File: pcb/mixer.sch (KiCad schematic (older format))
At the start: 59 parts, among them J18 Conn_Coaxial, J19 Conn_Coaxial, T1 Transformer_1P_SS, T2 Transformer_1P_SS, T3 Transformer_1P_SS, T4 Transformer_1P_SS, U4 TLV3542IDR

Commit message: layout progress
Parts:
- J18, J19: footprint Connector_Coaxial:SMA_Amphenol_132289_EdgeMount -> Connector_Coaxial:SMA_Samtec_SMA-J-P-X-ST-EM1_EdgeMount
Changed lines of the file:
@@
 F 0 "J18" H 6428 2488 50  0000 C CNN
 F 1 "Conn_Coaxial" H 6428 2397 50  0000 C CNN
-F 2 "Connector_Coaxial:SMA_Amphenol_132289_EdgeMount" H 6500 2250 50  0001 C CNN
+F 2 "Connector_Coaxial:SMA_Samtec_SMA-J-P-X-ST-EM1_EdgeMount" H 6500 2250 50  0001 C CNN
 F 3 " ~" H 6500 2250 50  0001 C CNN
 	1    6500 2250
@@
 F 0 "J19" H 6828 5338 50  0000 C CNN
 F 1 "Conn_Coaxial" H 6828 5247 50  0000 C CNN
-F 2 "Connector_Coaxial:SMA_Amphenol_132289_EdgeMount" H 6900 5100 50  0001 C CNN
+F 2 "Connector_Coaxial:SMA_Samtec_SMA-J-P-X-ST-EM1_EdgeMount" H 6900 5100 50  0001 C CNN
 F 3 " ~" H 6900 5100 50  0001 C CNN
 	1    6900 5100

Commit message: Add SMA step model
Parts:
- J18, J19: footprint Connector_Coaxial:SMA_Samtec_SMA-J-P-X-ST-EM1_EdgeMount -> iq_siggen:SMA_Samtec_SMA-J-P-X-ST-EM1_EdgeMount_withSTEP
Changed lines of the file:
@@
 F 0 "J18" H 6428 2488 50  0000 C CNN
 F 1 "Conn_Coaxial" H 6428 2397 50  0000 C CNN
-F 2 "Connector_Coaxial:SMA_Samtec_SMA-J-P-X-ST-EM1_EdgeMount" H 6500 2250 50  0001 C CNN
+F 2 "iq_siggen:SMA_Samtec_SMA-J-P-X-ST-EM1_EdgeMount_withSTEP" H 6500 2250 50  0001 C CNN
 F 3 " ~" H 6500 2250 50  0001 C CNN
 	1    6500 2250
@@
 F 0 "J19" H 6828 5338 50  0000 C CNN
 F 1 "Conn_Coaxial" H 6828 5247 50  0000 C CNN
-F 2 "Connector_Coaxial:SMA_Samtec_SMA-J-P-X-ST-EM1_EdgeMount" H 6900 5100 50  0001 C CNN
+F 2 "iq_siggen:SMA_Samtec_SMA-J-P-X-ST-EM1_EdgeMount_withSTEP" H 6900 5100 50  0001 C CNN
 F 3 " ~" H 6900 5100 50  0001 C CNN
 	1    6900 5100

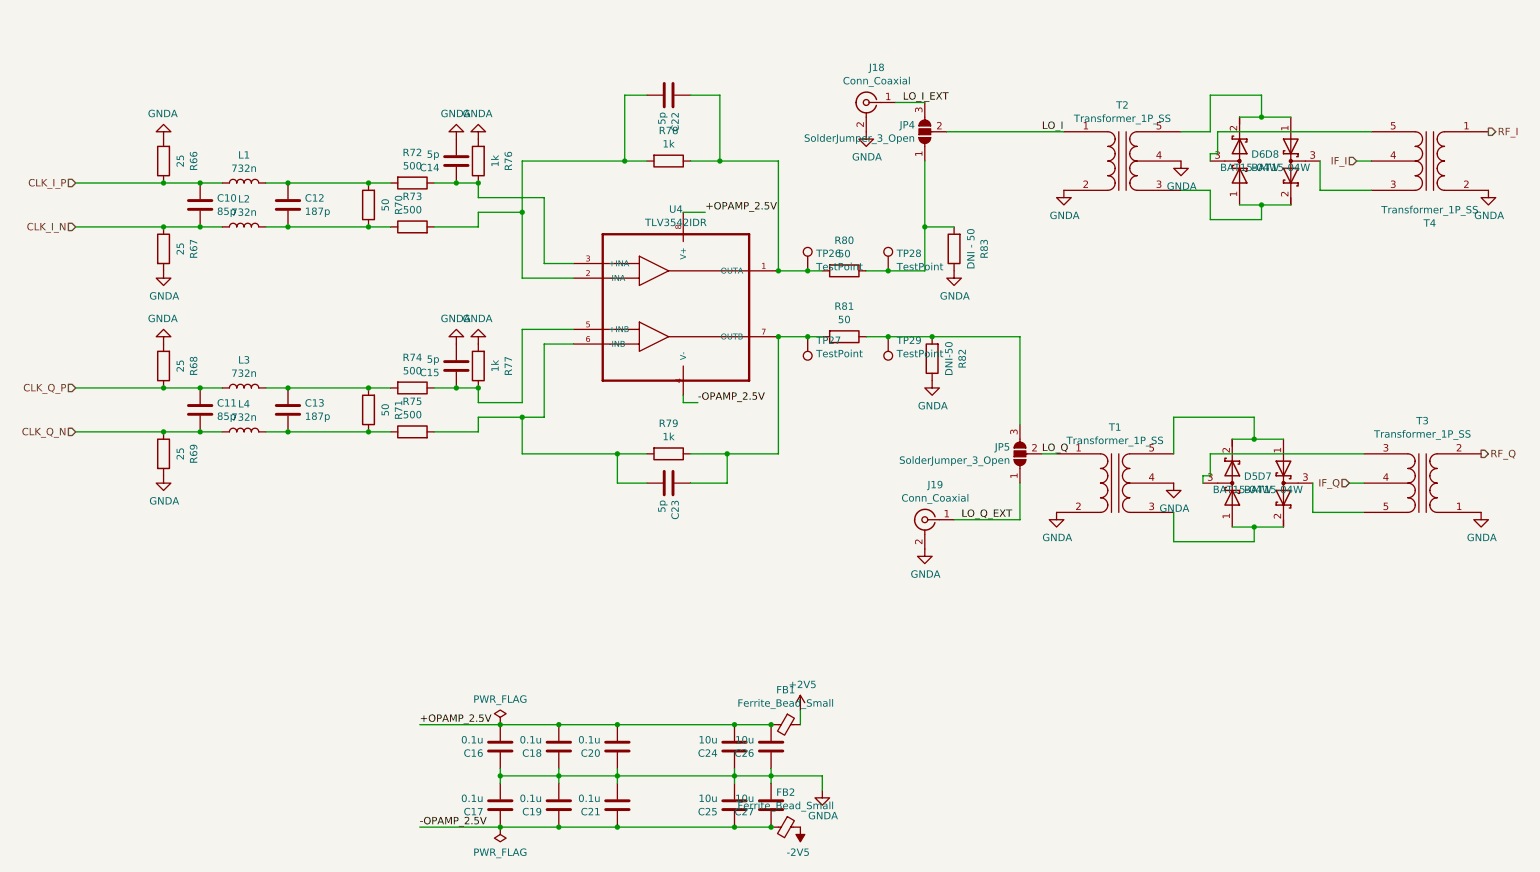
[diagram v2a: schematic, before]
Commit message: LO amp routing
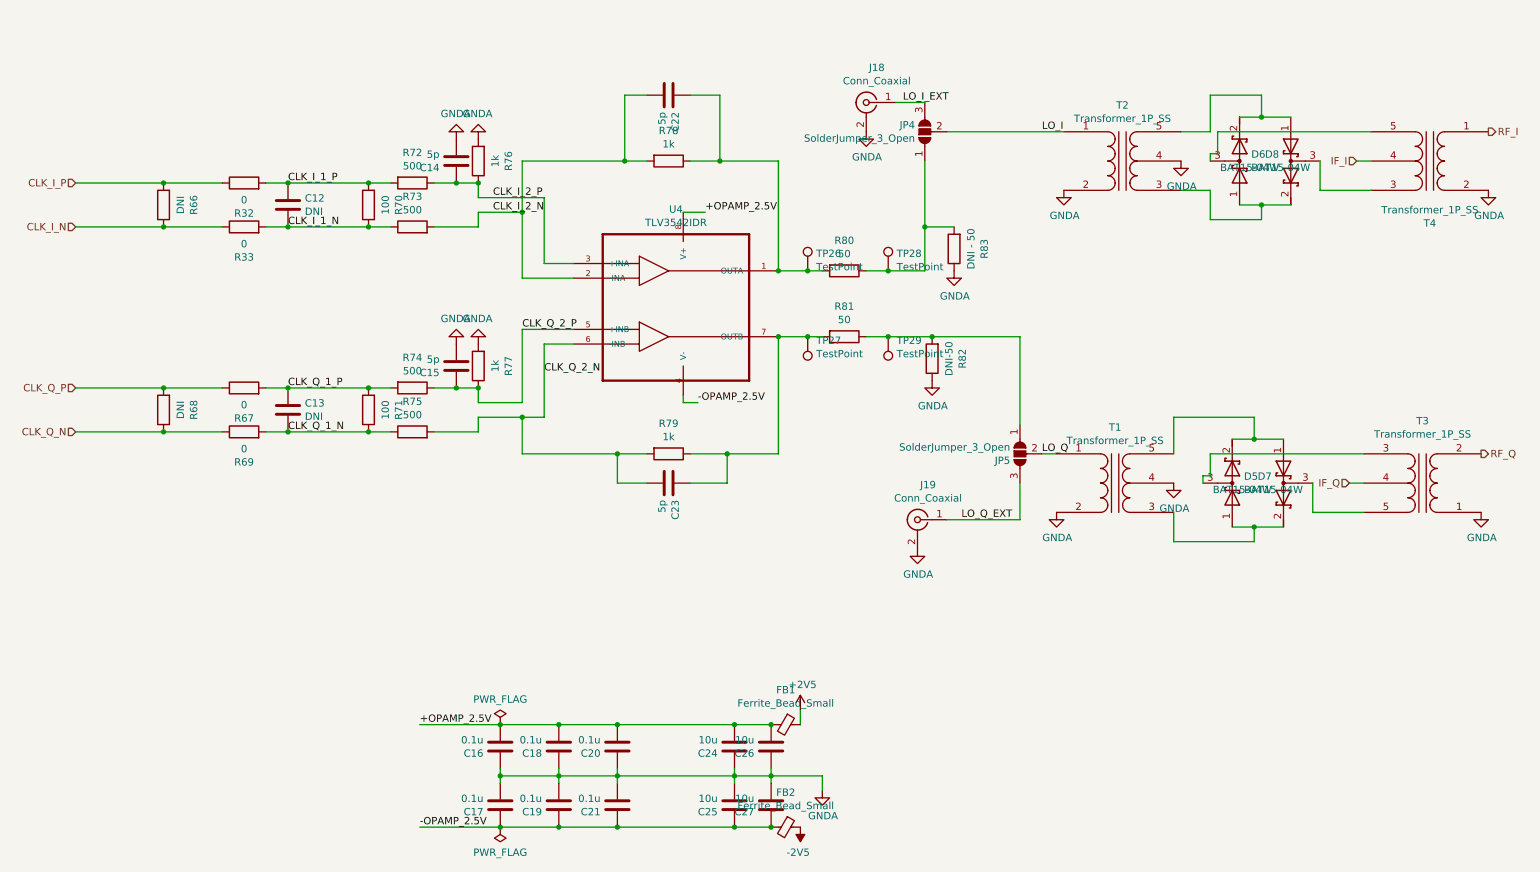
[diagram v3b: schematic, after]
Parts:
- removed C10, C11: 85p, Capacitor_SMD:C_0603_1608Metric, symbol Device:C
- removed L1, L2, L3, L4: 732n, Inductor_SMD:L_0603_1608Metric_Pad1.05x0.95mm_HandSolder, symbol Device:L
- added R32, R33: 0, Resistor_SMD:R_0603_1608Metric, symbol Device:R
- C12, C13: value 187p -> DNI
- JP4, JP5: footprint (none) -> iq_siggen:50ohm_solder_jumper
- R66, R68: value 25 -> DNI
- R67, R69: value 25 -> 0
- R70, R71: value 50 -> 100
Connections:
- net CLK_I_N: now also R66.1, R33.1; no longer R67.1
- net CLK_I_P: now also R66.2, R32.1; no longer R66.1
- net CLK_Q_N: now also R68.1
- net CLK_Q_P: now also R67.1, R68.2; no longer R68.1
- net GNDA: no longer R66.2, R67.2, R68.2, R69.2
- net LO_Q_EXT: now also JP5.3 (B); no longer JP5.1 (A)
- net CLK_I_2_N: now reaches C22.2, R73.2, R78.2, U4.2 (-INA)
- net CLK_I_2_P: now reaches C14.1, R72.1, R76.1, U4.3 (+INA)
- net CLK_Q_2_P: now reaches C15.1, R74.1, R77.1, U4.5 (+INB)
- net CLK_Q_2_N: now reaches C23.2, R75.2, R79.2, U4.6 (-INB)
- net CLK_I_1_N: now reaches C12.2, R70.1, R73.1
- net CLK_I_1_N: now also R33.2
- net CLK_I_1_P: now reaches C12.1, R70.2, R72.2
- net CLK_I_1_P: now also R32.2
- net CLK_Q_1_N: now reaches C13.2, R71.1, R75.1
- net CLK_Q_1_N: now also R69.2
- net CLK_Q_1_P: now reaches C13.1, R71.2, R74.2
- net CLK_Q_1_P: now also R67.2
- net at R81.1, R82.2, TP29.1: now also JP5.1 (A); no longer JP5.3 (B)
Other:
- moved on the sheet: J19, R66, R68

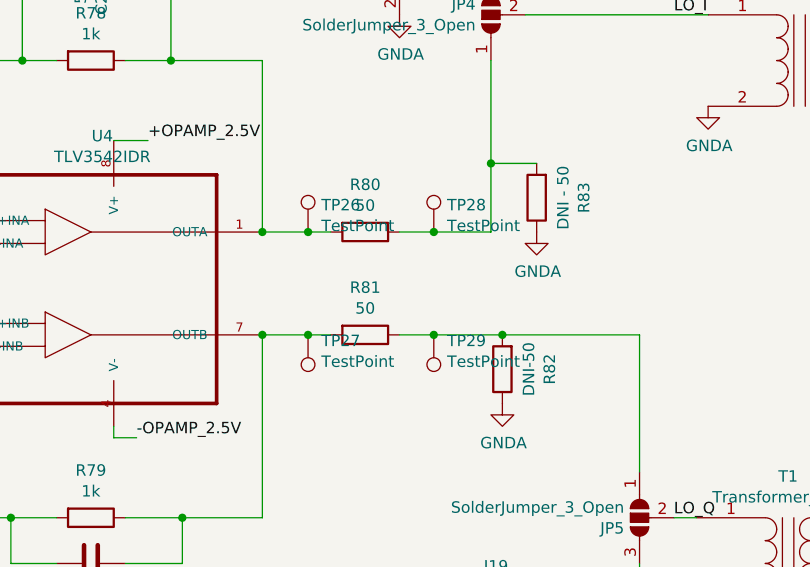
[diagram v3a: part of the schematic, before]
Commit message: clean up LO driver routing
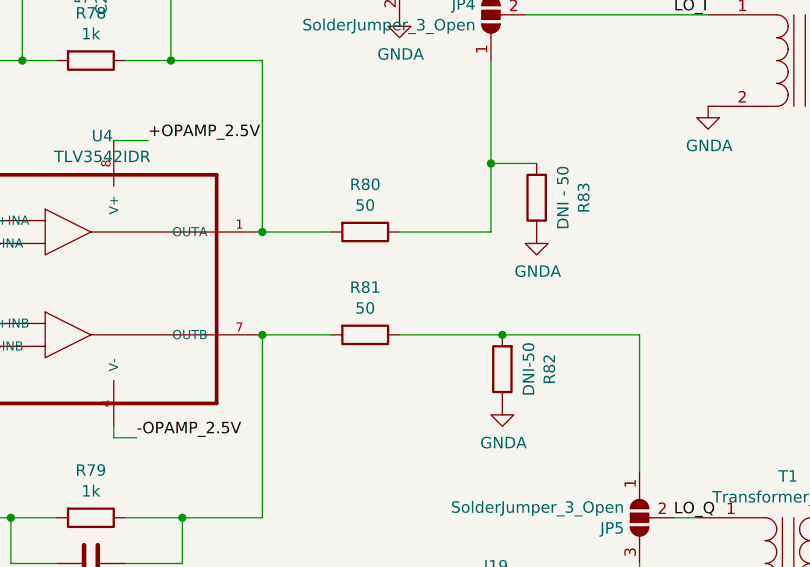
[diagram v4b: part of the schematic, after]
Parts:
- removed TP26, TP27, TP28, TP29: TestPoint, TestPoint:TestPoint_Pad_D1.5mm, symbol Connector:TestPoint
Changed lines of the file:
@@
 Text HLabel 10700 4650 2    50   Output ~ 0
 RF_Q
-Wire Wire Line
-	5900 3850 6100 3850
 Connection ~ 5900 3850
-Wire Wire Line
-	5900 3400 6100 3400
 Connection ~ 5900 3400
 Text Label 7700 2450 0    50   ~ 0
@@
 	0    1    1    0
 $EndComp
-Wire Wire Line
-	6500 3400 6650 3400
 $Comp
 L Device:R R?
@@
 	0    1    1    0
 $EndComp
-Wire Wire Line
-	6500 3850 6650 3850
 $Comp
 L power:GNDA #PWR?
@@
 	1    0    0    -1
 $EndComp
-$Comp
-L Connector:TestPoint TP26
-U 1 1 60A10865
-P 6100 3400
-F 0 "TP26" H 6158 3518 50  0000 L CNN
-F 1 "TestPoint" H 6158 3427 50  0000 L CNN
-F 2 "TestPoint:TestPoint_Pad_D1.5mm" H 6300 3400 50  0001 C CNN
-F 3 "~" H 6300 3400 50  0001 C CNN
-	1    6100 3400
-	1    0    0    -1
-$EndComp
-Connection ~ 6100 3400
-Wire Wire Line
-	6100 3400 6200 3400
-$Comp
-L Connector:TestPoint TP28
-U 1 1 60A10D60
-P 6650 3400
-F 0 "TP28" H 6708 3518 50  0000 L CNN
-F 1 "TestPoint" H 6708 3427 50  0000 L CNN
-F 2 "TestPoint:TestPoint_Pad_D1.5mm" H 6850 3400 50  0001 C CNN
-F 3 "~" H 6850 3400 50  0001 C CNN
-	1    6650 3400
-	1    0    0    -1
-$EndComp
-Connection ~ 6650 3400
-Wire Wire Line
-	6650 3400 6900 3400
-$Comp
-L Connector:TestPoint TP29
-U 1 1 60A10F72
-P 6650 3850
-F 0 "TP29" H 6592 3876 50  0000 R CNN
-F 1 "TestPoint" H 6592 3967 50  0000 R CNN
-F 2 "TestPoint:TestPoint_Pad_D1.5mm" H 6850 3850 50  0001 C CNN
-F 3 "~" H 6850 3850 50  0001 C CNN
-	1    6650 3850
-	-1   0    0    1
-$EndComp
-Connection ~ 6650 3850
-Wire Wire Line
-	6650 3850 6950 3850
-$Comp
-L Connector:TestPoint TP27
-U 1 1 60A1186F
-P 6100 3850
-F 0 "TP27" H 6042 3876 50  0000 R CNN
-F 1 "TestPoint" H 6042 3967 50  0000 R CNN
-F 2 "TestPoint:TestPoint_Pad_D1.5mm" H 6300 3850 50  0001 C CNN
-F 3 "~" H 6300 3850 50  0001 C CNN
-	1    6100 3850
-	-1   0    0    1
-$EndComp
-Connection ~ 6100 3850
-Wire Wire Line
-	6100 3850 6200 3850
 $Comp
 L Device:R R?
@@
 Text Label 4300 4100 0    50   ~ 0
 CLK_Q_2_N
+Wire Wire Line
+	5900 3400 6200 3400
+Wire Wire Line
+	6500 3400 6900 3400
+Wire Wire Line
+	6500 3850 6950 3850
+Wire Wire Line
+	5900 3850 6200 3850
 $EndSCHEMATC

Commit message: clean up, label sub circuit blocks in silkscreen document the expected clock and baseband amplitudes based on opamp gains
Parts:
- R76, R77, R78, R79: value 1k -> 1.5k
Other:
- note added: "gain = 1500/500 = 3"
- note added: "unterminated pk-pk amplitude = 2.1V\nterminated pk-pk = 1.05V"
- note added: "when terminated:\n+/- 350mV differential \n1.25V common mode voltage"
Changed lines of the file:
@@
 AR Path="/5FB04C67/5FB8535E" Ref="R78"  Part="1"
 F 0 "R78" V 4943 2650 50  0000 C CNN
-F 1 "1k" V 5034 2650 50  0000 C CNN
+F 1 "1.5k" V 5034 2650 50  0000 C CNN
 F 2 "Resistor_SMD:R_0603_1608Metric" V 5080 2650 50  0001 C CNN
 F 3 "~" H 5150 2650 50  0001 C CNN
@@
 AR Path="/5FB04C67/5FB85364" Ref="R76"  Part="1"
 F 0 "R76" V 3643 2650 50  0000 C CNN
-F 1 "1k" V 3734 2650 50  0000 C CNN
+F 1 "1.5k" V 3734 2650 50  0000 C CNN
 F 2 "Resistor_SMD:R_0603_1608Metric" V 3780 2650 50  0001 C CNN
 F 3 "~" H 3850 2650 50  0001 C CNN
@@
 AR Path="/5FB04C67/5FB8539E" Ref="R77"  Part="1"
 F 0 "R77" V 3643 4050 50  0000 C CNN
-F 1 "1k" V 3734 4050 50  0000 C CNN
+F 1 "1.5k" V 3734 4050 50  0000 C CNN
 F 2 "Resistor_SMD:R_0603_1608Metric" V 3780 4050 50  0001 C CNN
 F 3 "~" H 3850 4050 50  0001 C CNN
@@
 AR Path="/5FB04C67/5FB853BB" Ref="R79"  Part="1"
 F 0 "R79" V 4943 4650 50  0000 C CNN
-F 1 "1k" V 5034 4650 50  0000 C CNN
+F 1 "1.5k" V 5034 4650 50  0000 C CNN
 F 2 "Resistor_SMD:R_0603_1608Metric" V 5080 4650 50  0001 C CNN
 F 3 "~" H 5150 4650 50  0001 C CNN
@@
 Wire Wire Line
 	5900 3850 6200 3850
+Text Notes 2100 2500 0    50   ~ 0
+when terminated:\n+/- 350mV differential \n1.25V common mode voltage
+Wire Notes Line
+	3100 2700 3100 2550
+Text Notes 4450 1800 0    50   ~ 0
+gain = 1500/500  = 3
+Text Notes 6900 1800 0    50   ~ 0
+unterminated pk-pk amplitude = 2.1V\nterminated pk-pk = 1.05V
 $EndSCHEMATC

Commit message: populate LCSC BOM for JLCPCB assembly
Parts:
- C14, C15, C22, C23: value 5p -> 4.7p; LCSC (none) -> C1669
- C16, C17, C18, C19, C20, C21: LCSC (none) -> C14663
- C24, C25, C26, C27: LCSC (none) -> C19702
- FB1, FB2: LCSC (none) -> C19330
- R32, R33, R67, R69: LCSC (none) -> C21189
- R70, R71: LCSC (none) -> C22775
- R72, R73, R74, R75: value 500 -> 499; LCSC (none) -> C23065
- R76, R77, R78, R79: LCSC (none) -> C22843
- R80, R81: value 50 -> 49.9; LCSC (none) -> C23185
